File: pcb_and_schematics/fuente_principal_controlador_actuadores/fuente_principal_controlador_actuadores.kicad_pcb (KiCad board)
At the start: 2 copper layers, 166.5 x 108.5 mm, 78 parts, among them J1 Screw_Terminal_01x02, J10 Screw_Terminal_01x02, J11 Conn_01x15_Female, J12 Conn_01x15_Female, J2 Screw_Terminal_01x02, J3 Screw_Terminal_01x02, J4 Screw_Terminal_01x02, J5 Screw_Terminal_01x02, J6 Screw_Terminal_01x02, J7 Screw_Terminal_01x02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

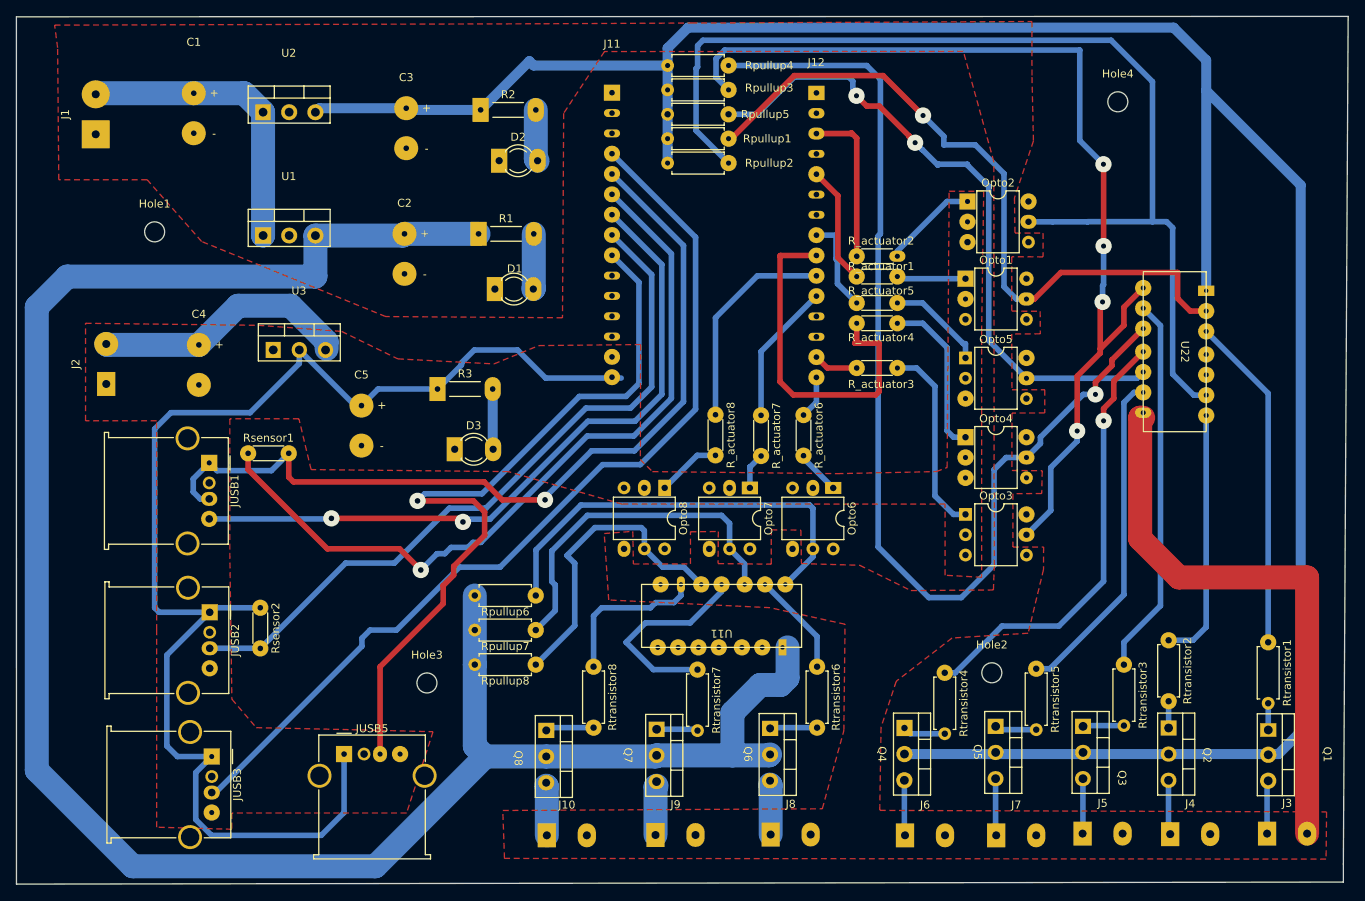
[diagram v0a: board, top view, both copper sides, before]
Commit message: little fixies, only remains to check for the horizontal spacing of the esp32 of 30 pins used here
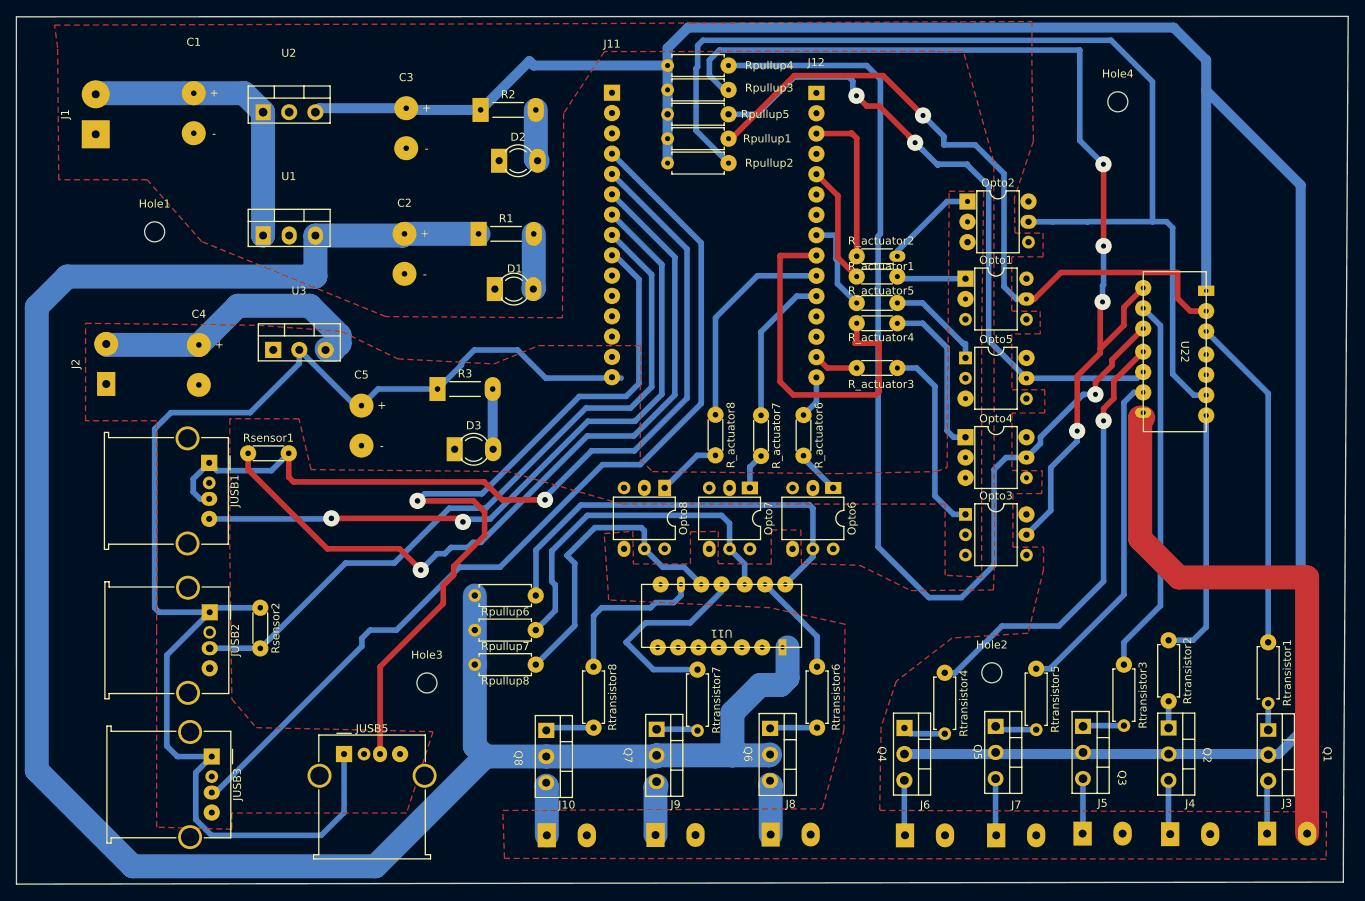
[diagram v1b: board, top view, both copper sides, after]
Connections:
- J12 pad 4: (no net) -> unconnected-(J11-Pad3)
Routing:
- net Net-(C4-Pad1): track 32.4 -> 35.8 mm
- net mainWaterPump: track 17.8 -> 19.2 mm
- net Net-(Opto3-Pad5): track 126.1 -> 127.5 mm
- net signal PH: track 117.2 -> 117.8 mm

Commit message: fix of pad size of some resistors and other elements
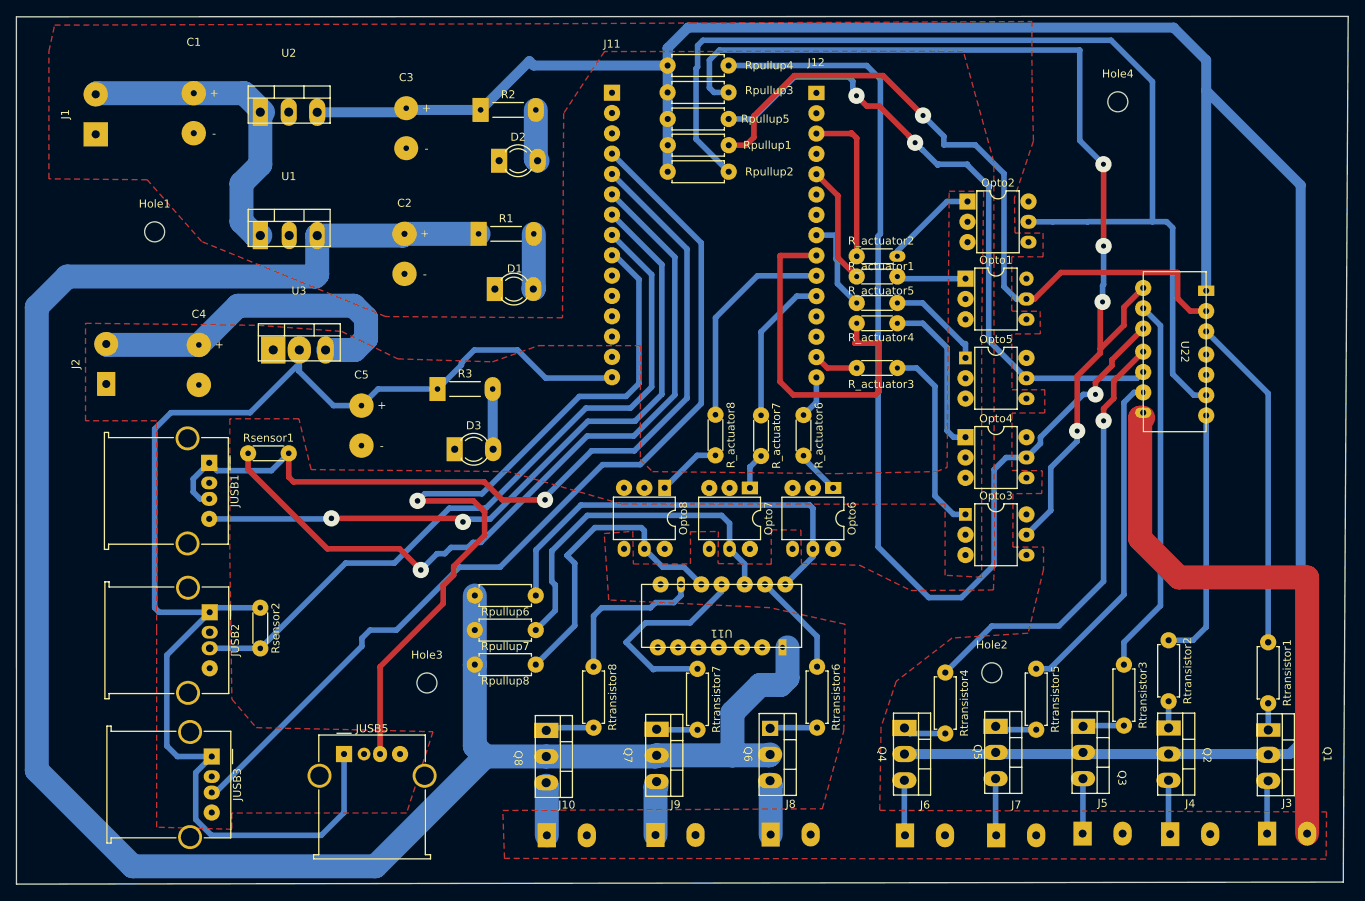
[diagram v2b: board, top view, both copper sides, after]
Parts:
- moved Rpullup2 1.09 mm to (123.8, 43.3)
- moved Rpullup1 0.81 mm to (123.8, 40.0)
- moved Rpullup5 0.59 mm to (123.8, 36.7)
- moved Rpullup3 0.32 mm to (123.8, 33.4)
- moved Rtransistor7 0.10 mm to (119.9, 105.4)
- moved Rtransistor4 0.07 mm to (150.9, 105.9)
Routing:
- net Net-(C4-Pad1): track 35.8 -> 43.1 mm
- net Net-(C1-Pad1): track 37.4 -> 39.7 mm
- net Net-(Opto1-Pad5): track 88.7 -> 90.6 mm
- net 5.0VDC pot: track 296.1 -> 297.8 mm
- net Net-(Opto3-Pad5): track 127.5 -> 129.2 mm
- net Net-(Opto2-Pad5): track 135.1 -> 136.2 mm
- net Net-(Q4-Pad1): track 5.34 -> 6.41 mm
- net 3.3VDC: track 168.5 -> 169.0 mm
